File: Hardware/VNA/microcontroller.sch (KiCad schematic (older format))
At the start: 64 parts, among them SW1 SW_Push, SW2 SW_Push, SW3 SW_Push, U16 STM32F373RCTx, U17 AT25SF081-SSHD-X, Y1 8MHz

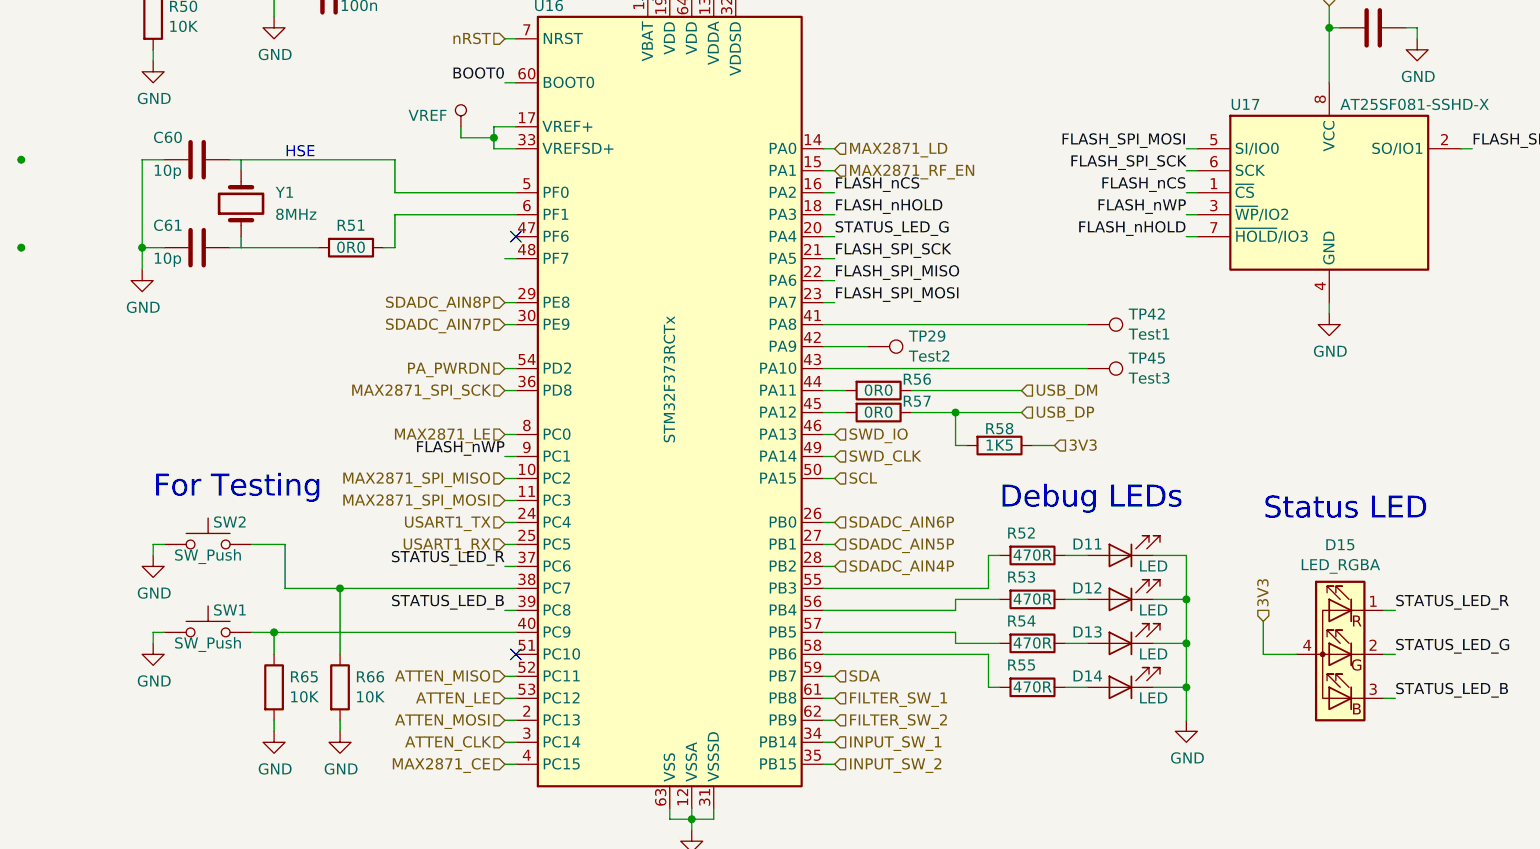
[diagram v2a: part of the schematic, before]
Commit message: bodge wire + 3 lines of code = usb works!
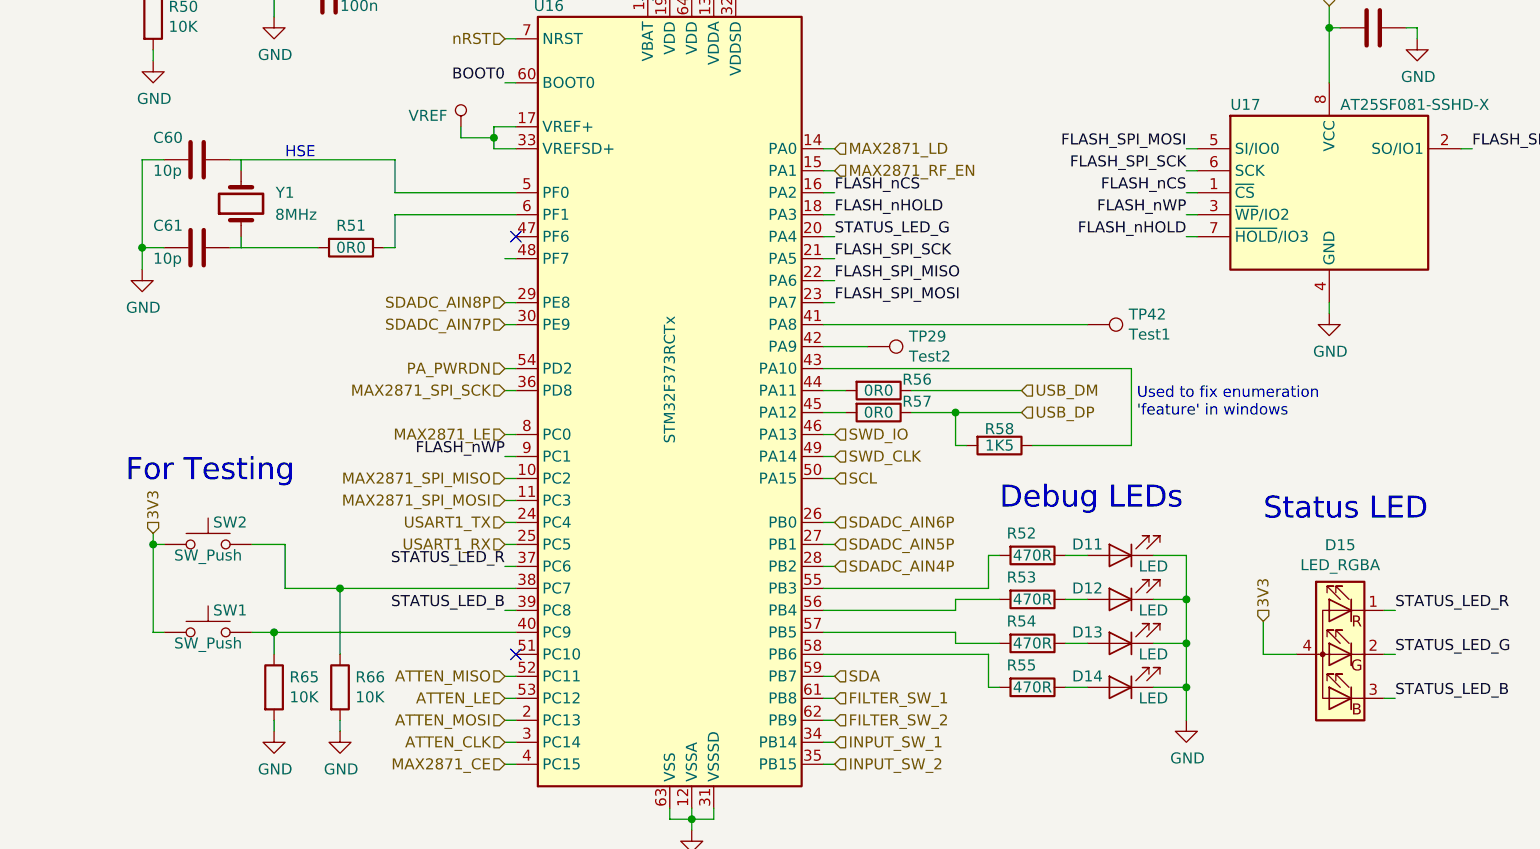
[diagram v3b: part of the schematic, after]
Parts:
- removed TP45: Test3, TestPoint:TestPoint_Pad_D1.0mm, symbol Connector:TestPoint
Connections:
- net GND: no longer SW1.1, SW2.1
- net VDD: now also SW1.1, SW2.1; no longer R58.1
- net at U16.43 (PA10): now also R58.1
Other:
- note added: "Used to fix enumeration \n'feature' in windows"
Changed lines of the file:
@@
 Wire Wire Line
 	1700 2750 1750 2750
-Connection ~ 50   2750
 Wire Wire Line
 	1400 2750 1050 2750
@@
 Text Notes 1250 2350 0    50   ~ 0
 HSE
-Connection ~ 50   2350
 Wire Wire Line
 	1750 2350 1050 2350
@@
 Text Notes 4500 3950 0    100  ~ 0
 Debug LEDs
-$Comp
-L power:GND #PWR098
-U 1 1 5CED3E6F
-P 650 4150
-F 0 "#PWR098" H 650 3900 50  0001 C CNN
-F 1 "GND" H 655 3977 50  0000 C CNN
-F 2 "" H 650 4150 50  0001 C CNN
-F 3 "" H 650 4150 50  0001 C CNN
-	1    650  4150
-	1    0    0    -1
-$EndComp
 Wire Wire Line
 	700  4100 650  4100
@@
 	1    0    0    -1
 $EndComp
-Wire Wire Line
-	650  4100 650  4150
-$Comp
-L power:GND #PWR099
-U 1 1 5CEF0A31
-P 650 4550
-F 0 "#PWR099" H 650 4300 50  0001 C CNN
-F 1 "GND" H 655 4377 50  0000 C CNN
-F 2 "" H 650 4550 50  0001 C CNN
-F 3 "" H 650 4550 50  0001 C CNN
-	1    650  4550
-	1    0    0    -1
-$EndComp
-Wire Wire Line
-	700  4500 650  4500
 $Comp
 L Switch:SW_Push SW2
@@
 $EndComp
 Wire Wire Line
-	650  4500 650  4550
-Wire Wire Line
 	1100 4500 1200 4500
 Wire Wire Line
@@
 Wire Wire Line
 	1250 4300 1500 4300
-Text Notes 650  3900 0    100  ~ 0
+Text Notes 525  3825 0    100  ~ 0
 For Testing
 Wire Wire Line
@@
 	0    1    1    0
 $EndComp
-Text HLabel 4750 3650 2    50   Input ~ 0
-3V3
 $Comp
 L Device:R R56
@@
 Wire Wire Line
 	4300 3500 4600 3500
-Wire Wire Line
-	4650 3650 4750 3650
 Text Label 8600 2400 2    50   ~ 0
 FLASH_SPI_MOSI
@@
 	1    0    0    -1
 $EndComp
-$Comp
-L Connector:TestPoint TP45
-U 1 1 5CBAC71B
-P 4900 3300
-F 0 "TP45" V 4854 3488 50  0000 L CNN
-F 1 "Test3" V 4945 3488 50  0000 L CNN
-F 2 "TestPoint:TestPoint_Pad_D1.0mm" H 5100 3300 50  0001 C CNN
-F 3 "~" H 5100 3300 50  0001 C CNN
-	1    4900 3300
-	0    1    1    0
-$EndComp
-Wire Wire Line
-	3700 3300 4900 3300
 Wire Wire Line
 	3700 3200 3900 3200
@@
 	0    1    1    0
 $EndComp
+Wire Wire Line
+	700  4500 650  4500
+Wire Wire Line
+	650  4500 650  4100
+Connection ~ 650  4100
+Wire Wire Line
+	650  4100 650  4050
+Text HLabel 650  4050 1    50   Input ~ 0
+3V3
+Wire Wire Line
+	5100 3650 5100 3300
+Wire Wire Line
+	4650 3650 5100 3650
+Wire Wire Line
+	3700 3300 5100 3300
+Text Notes 5125 3525 0    50   ~ 0
+Used to fix enumeration \n'feature' in windows
 $EndSCHEMATC
